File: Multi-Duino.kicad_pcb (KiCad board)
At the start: 4 copper layers, 68.6 x 53.3 mm, 67 parts, among them J1 M20-9980345, J10 Micro_SD_Card_Det1, J2 M20-9980245, J3 M20-9980345, J4 PPTC101LFBN-RC, J5 PPTC081LFBN-RC, J6 PPTC061LFBN-RC, J7 PPTC081LFBN-RC, J8 USB_C_Receptacle_USB2.0_16P, Q1 FDN340P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

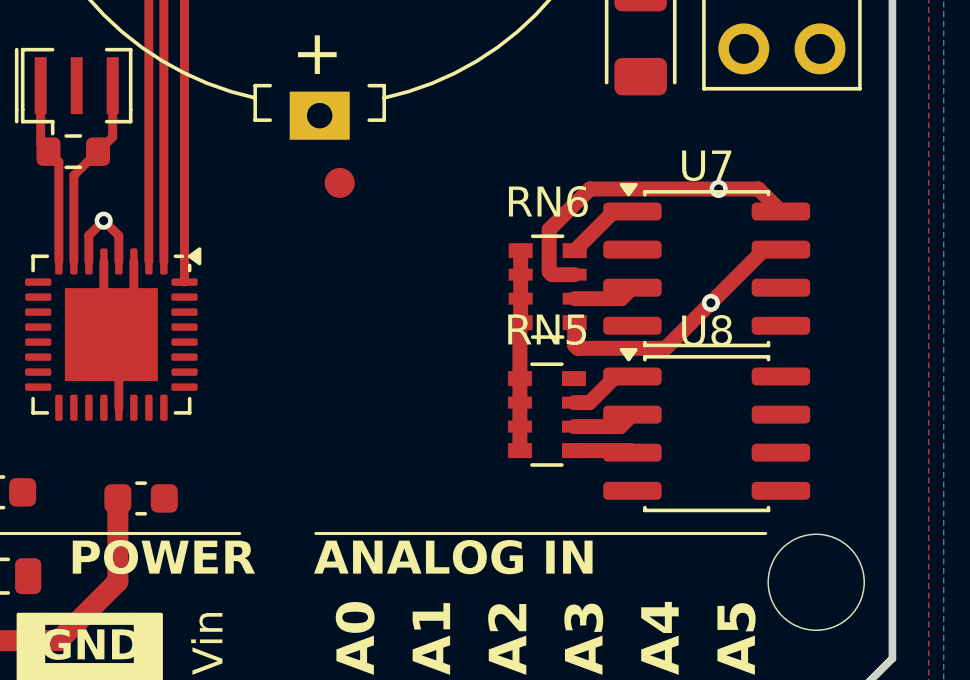
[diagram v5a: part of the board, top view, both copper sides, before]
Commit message: Update Multiduino v2 design
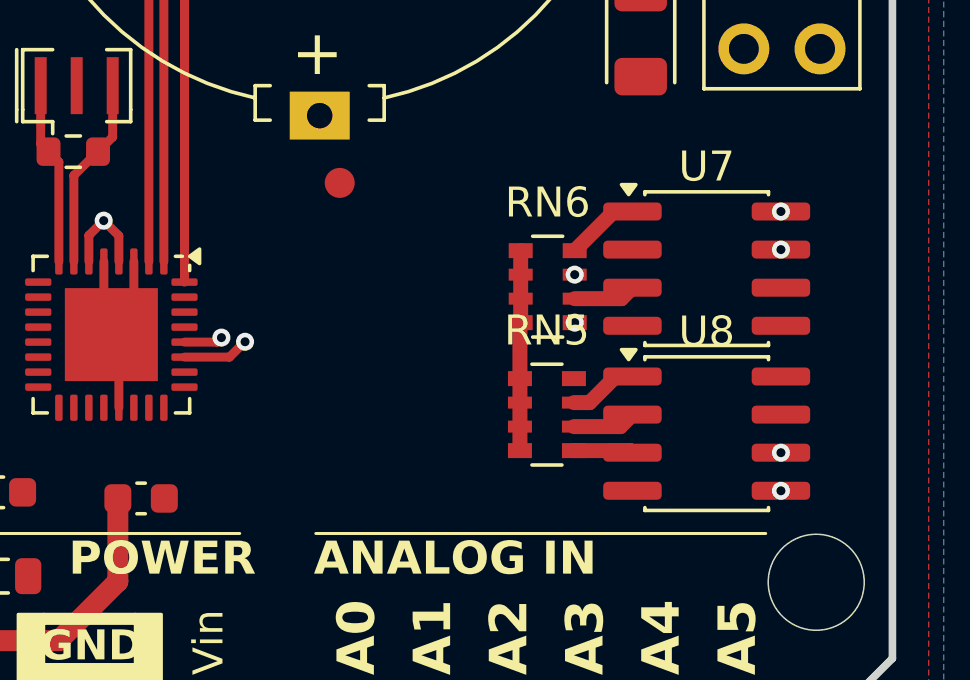
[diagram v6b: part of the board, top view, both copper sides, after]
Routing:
- net A5/SCL: track 10.9 -> 1.29 mm, vias 1 -> 4
- net A4/SDA: track 9.03 -> 2.31 mm, vias 1 -> 4
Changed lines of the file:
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@@
 	)
 	(segment
-		(start 176.741158 114.741158)
-		(end 178.517316 112.965)
-		(width 0.5)
+		(start 160.693801 116.5486)
+		(end 159.1936 116.5486)
+		(width 0.3)
 		(layer "F.Cu")
 		(net 34)
 	)
 	(segment
-		(start 172.2 116.15)
-		(end 172.305 116.255)
-		(width 0.5)
+		(start 161.074562 116.037432)
+		(end 161.074562 116.167839)
+		(width 0.3)
 		(layer "F.Cu")
 		(net 34)
 	)
 	(segment
-		(start 175.227316 116.255)
-		(end 176.741158 114.741158)
-		(width 0.5)
+		(start 161.212426 116.037432)
+		(end 161.074562 116.037432)
+		(width 0.3)
 		(layer "F.Cu")
 		(net 34)
 	)
 	(segment
-		(start 172.305 116.255)
-		(end 175.227316 116.255)
-		(width 0.5)
-		(layer "F.Cu")
-		(net 34)
-	)
-	(segment
-		(start 172.2 115.4)
-		(end 172.2 116.15)
-		(width 0.5)
-		(layer "F.Cu")
-		(net 34)
-	)
-	(segment
-		(start 178.517316 112.965)
-		(end 179.075 112.965)
-		(width 0.5)
+		(start 161.074562 116.167839)
+		(end 160.693801 116.5486)
+		(width 0.3)
 		(layer "F.Cu")
 		(net 34)
 	)
 	(via
-		(at 176.741158 114.741158)
+		(at 172.2 115.4)
+		(size 0.6)
+		(drill 0.3)
+		(layers "F.Cu" "B.Cu")
+		(net 34)
+	)
+	(via
+		(at 161.212426 116.037432)
+		(size 0.6)
+		(drill 0.3)
+		(layers "F.Cu" "B.Cu")
+		(net 34)
+	)
+	(via
+		(at 179.075 112.965)
+		(size 0.6)
+		(drill 0.3)
+		(layers "F.Cu" "B.Cu")
+		(net 34)
+	)
+	(via
+		(at 179.075 121.005)
 		(size 0.6)
 		(drill 0.3)
@@
 	)
 	(segment
-		(start 178.325 110.945)
-		(end 179.075 111.695)
-		(width 0.5)
+		(start 160.274562 116.0486)
+		(end 159.1936 116.0486)
+		(width 0.3)
 		(layer "F.Cu")
 		(net 36)
 	)
 	(segment
-		(start 171.35 113.7)
-		(end 171.35 112.3)
-		(width 0.5)
-		(layer "F.Cu")
-		(net 36)
-	)
-	(segment
-		(start 172.705 110.945)
-		(end 177 110.945)
-		(width 0.5)
-		(layer "F.Cu")
-		(net 36)
-	)
-	(segment
-		(start 177 110.945)
-		(end 178.325 110.945)
-		(width 0.5)
-		(layer "F.Cu")
-		(net 36)
-	)
-	(segment
-		(start 172.2 113.8)
-		(end 171.45 113.8)
-		(width 0.5)
-		(layer "F.Cu")
-		(net 36)
-	)
-	(segment
-		(start 171.35 112.3)
-		(end 172.705 110.945)
-		(width 0.5)
-		(layer "F.Cu")
-		(net 36)
-	)
-	(segment
-		(start 171.45 113.8)
-		(end 171.35 113.7)
-		(width 0.5)
+		(start 160.424562 115.8986)
+		(end 160.274562 116.0486)
+		(width 0.3)
 		(layer "F.Cu")
 		(net 36)
 	)
 	(via
-		(at 177 110.945)
+		(at 160.424562 115.8986)
 		(size 0.6)
 		(drill 0.3)
+		(layers "F.Cu" "B.Cu")
+		(net 36)
+	)
+	(via
+		(at 172.2 113.8)
+		(size 0.6)
+		(drill 0.3)
+		(layers "F.Cu" "B.Cu")
+		(net 36)
+	)
+	(via
+		(at 179.075 111.695)
+		(size 0.6)
+		(drill 0.3)
+		(layers "F.Cu" "B.Cu")
+		(net 36)
+	)
+	(via
+		(at 179.075 119.735)
+		(size 0.6)
+		(drill 0.3)

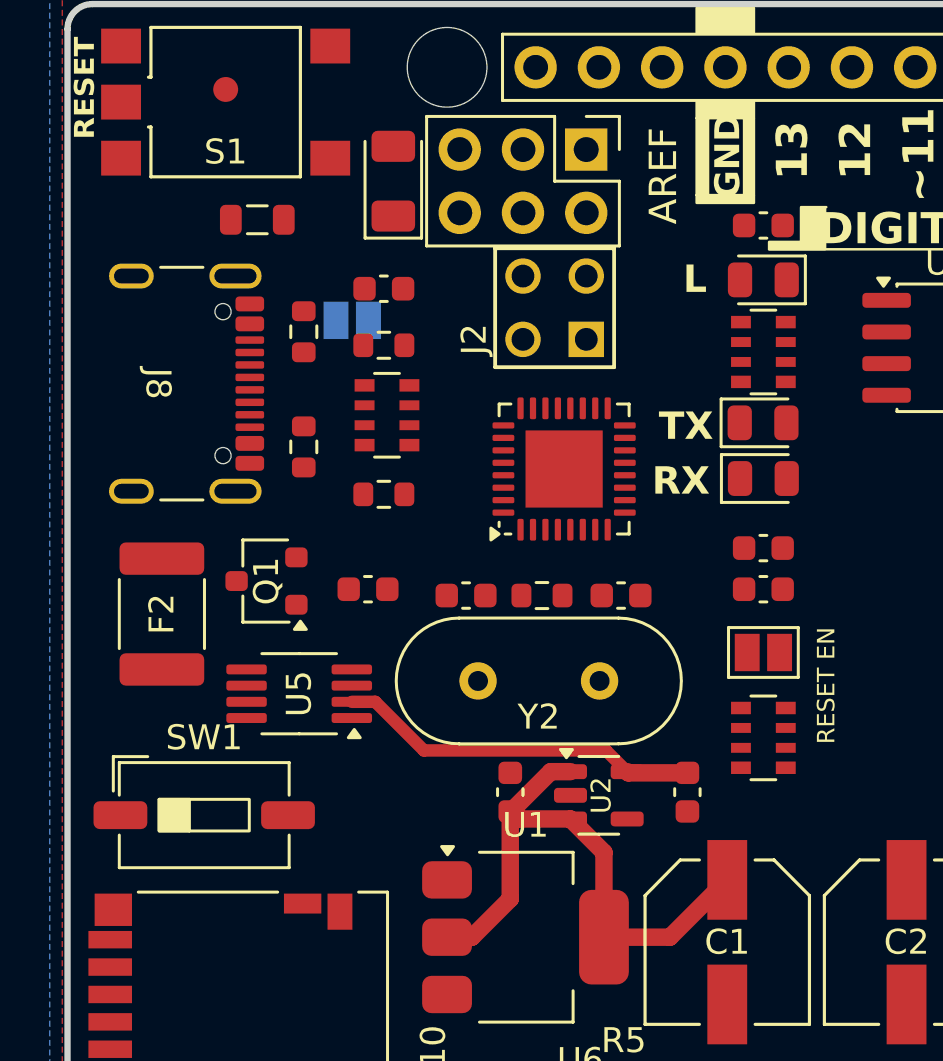
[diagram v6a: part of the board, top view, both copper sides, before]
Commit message: Update Multiduino v2 design
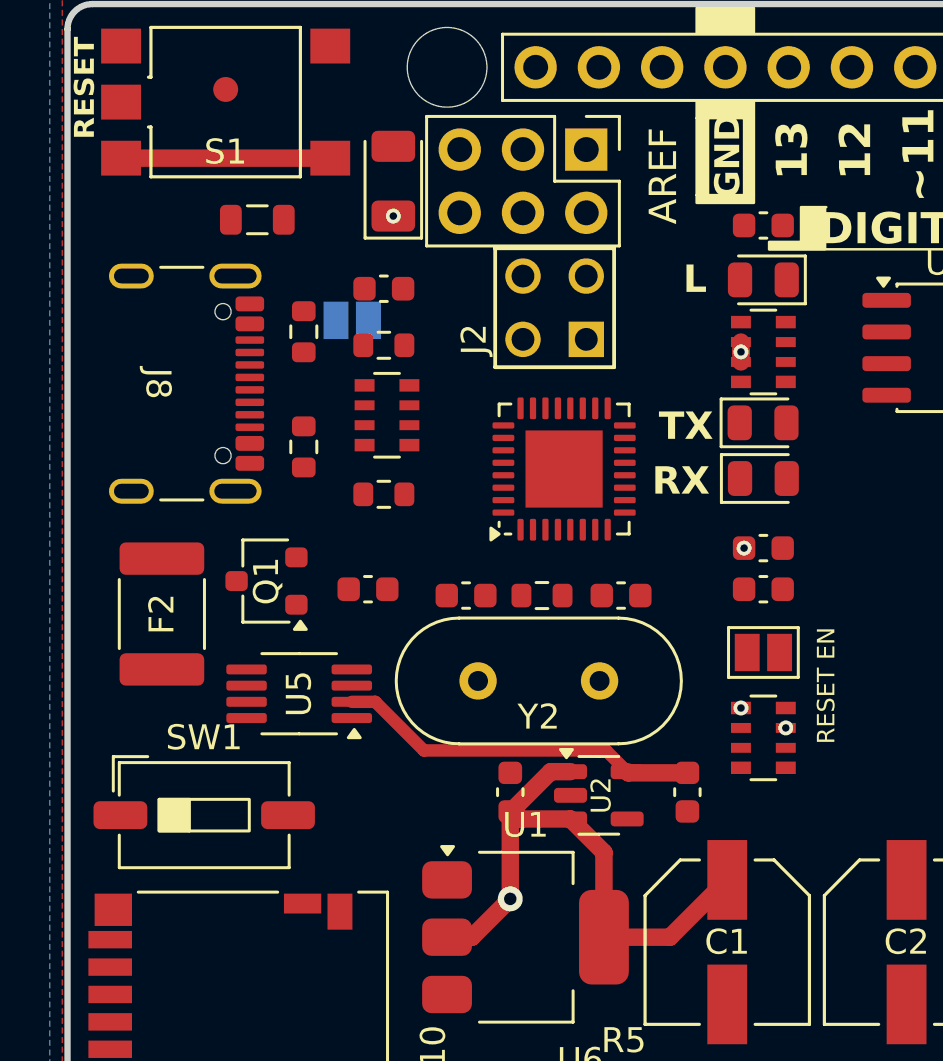
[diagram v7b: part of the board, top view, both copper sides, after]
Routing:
- net RESET: track 0.00 -> 8.40 mm
- net +5V: track 47.0 -> 47.8 mm, vias 1 -> 7
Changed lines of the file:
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@@
+	)
+	(segment
+		(start 141.2511 91.9036)
+		(end 141.2511 92.3)
+		(width 0.7)
+		(layer "F.Cu")
+		(net 2)
 	)
 	(segment
@@
 	)
 	(segment
+		(start 141.2511 92.3)
+		(end 141.2511 92.7036)
+		(width 0.7)
+		(layer "F.Cu")
+		(net 2)
+	)
+	(segment
 		(start 170.4 113.8)
 		(end 170.4 113)
@@
 	)
 	(via
+		(at 141.2511 106.5976)
+		(size 0.6)
+		(drill 0.3)
+		(layers "F.Cu" "B.Cu")
+		(net 2)
+	)
+	(via
+		(at 143.0511 107.3976)
+		(size 0.6)
+		(drill 0.3)
+		(layers "F.Cu" "B.Cu")
+		(net 2)
+	)
+	(via
 		(at 156.5 112)
 		(size 0.6)
 		(drill 0.3)
+		(layers "F.Cu" "B.Cu")
+		(net 2)
+	)
+	(via
+		(at 141.3761 100.1776)
+		(size 0.6)
+		(drill 0.3)
+		(layers "F.Cu" "B.Cu")
+		(net 2)
+	)
+	(via
+		(at 141.2511 92.3)
+		(size 0.6)
+		(drill 0.3)
+		(layers "F.Cu" "B.Cu")
+		(net 2)
+	)
+	(via
+		(at 127.2921 86.8456)
+		(size 0.6)
+		(drill 0.3)
+		(layers "F.Cu" "B.Cu")
+		(net 2)
+	)
+	(via
+		(at 131.988 114.262)
+		(size 1)
+		(drill 0.5)
 		(layers "F.Cu" "B.Cu")
 		(net 2)
@@
 	)
 	(segment
+		(start 116.3611 84.5206)
+		(end 124.7611 84.5206)
+		(width 0.7)
+		(layer "F.Cu")
+		(net 6)
+	)
+	(segment

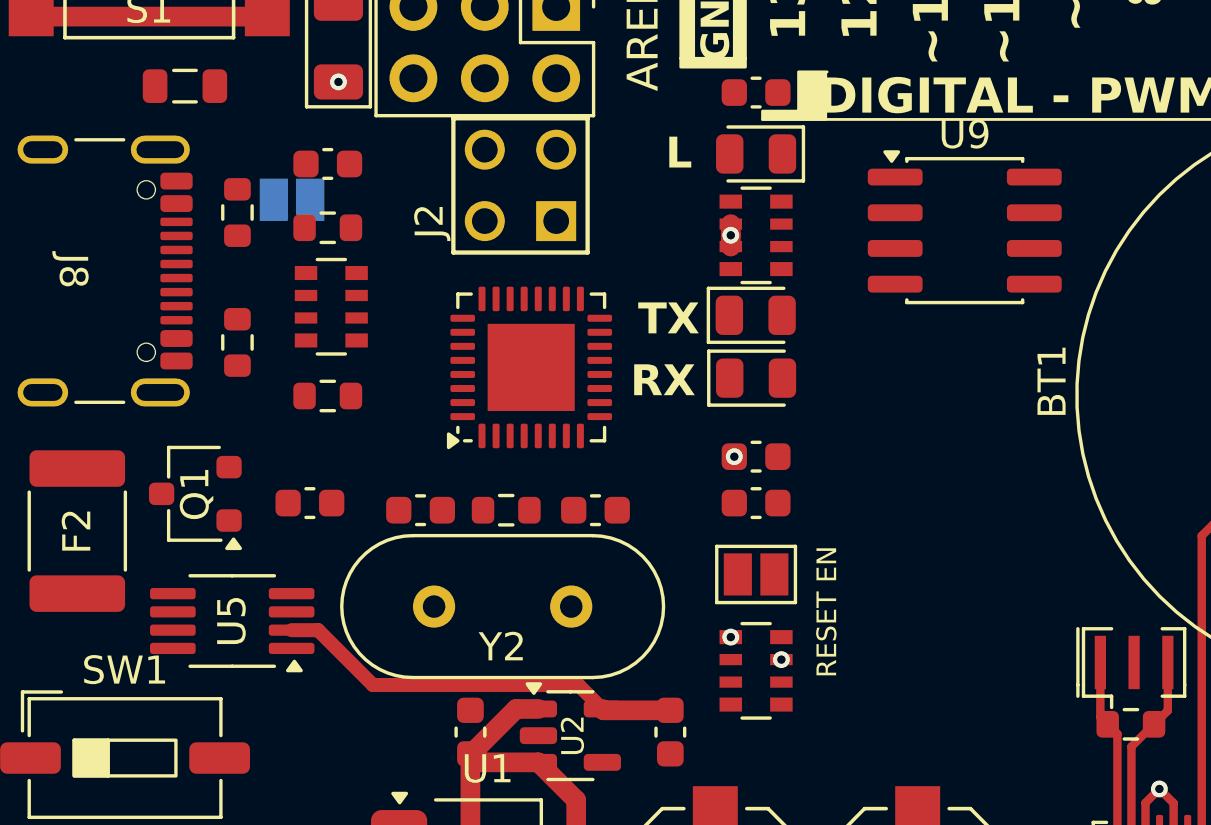
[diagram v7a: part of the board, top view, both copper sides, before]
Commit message: Update Multiduino v2 design
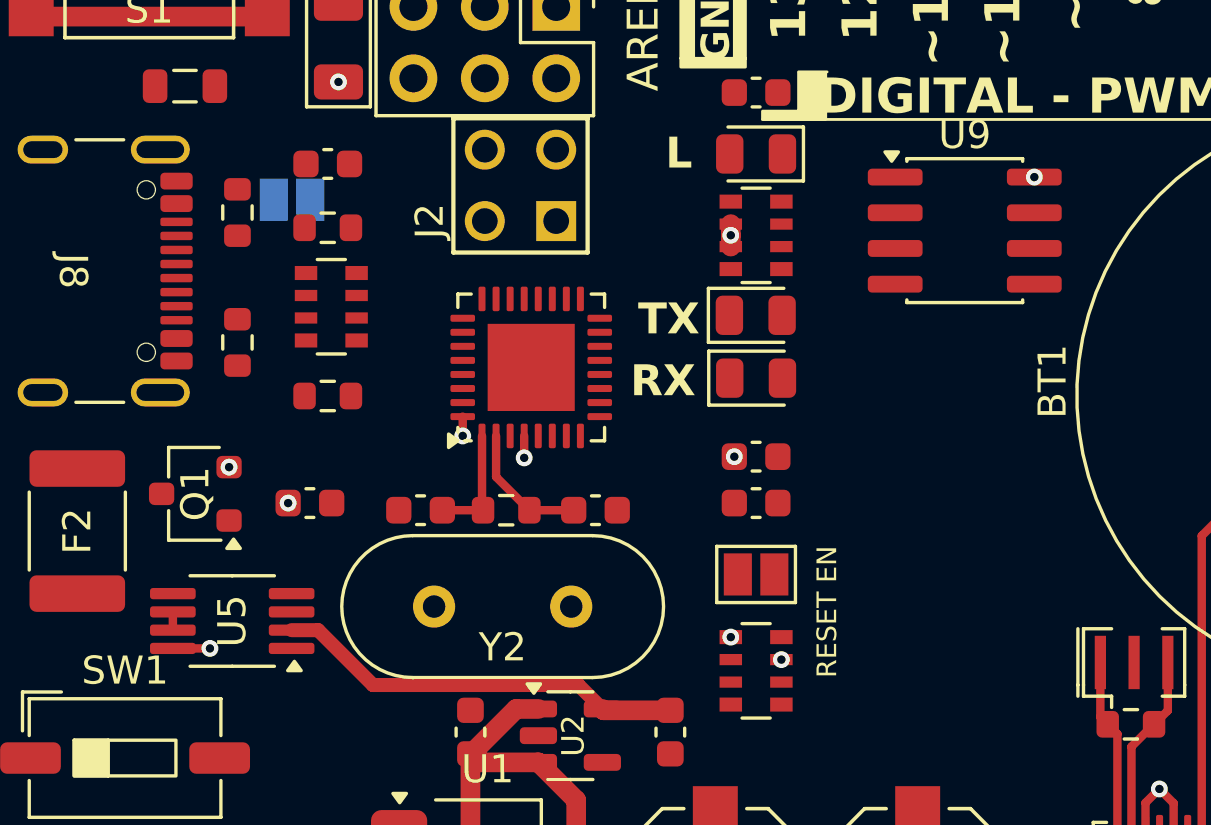
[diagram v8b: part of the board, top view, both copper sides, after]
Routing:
- net Net-(U3-PC0): track 0.00 -> 4.71 mm
- net Net-(U3-XTAL1): track 0.00 -> 4.11 mm
- net +5V: track 47.8 -> 50.6 mm, vias 7 -> 13
- net Net-(RN2A-R1.2): track 0.00 -> 0.65 mm
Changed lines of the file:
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@@
+	)
+	(segment
+		(start 122.72 107)
+		(end 121.4 107)
+		(width 0.3)
+		(layer "F.Cu")
+		(net 2)
 	)
 	(segment
@@
 	)
 	(segment
+		(start 133.9001 100.2201)
+		(end 133.9001 99.4401)
+		(width 0.3)
+		(layer "F.Cu")
+		(net 2)
+	)
+	(segment
 		(start 131.988 110.752)
 		(end 132.01525 110.752)
@@
 	)
 	(segment
+		(start 131.7126 99.44)
+		(end 131.7126 98.7526)
+		(width 0.3)
+		(layer "F.Cu")
+		(net 2)
+	)
+	(segment
 		(start 170.375 119.665)
 		(end 170.375 118.865)
@@
 	)
 	(via
+		(at 131.7126 99.44)
+		(size 0.6)
+		(drill 0.3)
+		(layers "F.Cu" "B.Cu")
+		(net 2)
+	)
+	(via
 		(at 141.2511 106.5976)
 		(size 0.6)
@@
 	)
 	(via
+		(at 123.4 100.55)
+		(size 0.6)
+		(drill 0.3)
+		(layers "F.Cu" "B.Cu")
+		(net 2)
+	)
+	(via
+		(at 122.72 107)
+		(size 0.6)
+		(drill 0.3)
+		(layers "F.Cu" "B.Cu")
+		(net 2)
+	)
+	(via
 		(at 141.3761 100.1776)
 		(size 0.6)
@@
 	)
 	(via
+		(at 133.9001 100.2201)
+		(size 0.6)
+		(drill 0.3)
+		(layers "F.Cu" "B.Cu")
+		(net 2)
+	)
+	(via
 		(at 127.2921 86.8456)
+		(size 0.6)
+		(drill 0.3)
+		(layers "F.Cu" "B.Cu")
+		(net 2)
+	)
+	(via
+		(at 152.05 90.23)
 		(size 0.6)
 		(drill 0.3)
@@
 		(net 2)
 	)
+	(via
+		(at 125.5011 101.8286)
+		(size 0.6)
+		(drill 0.3)
+		(layers "F.Cu" "B.Cu")
+		(net 2)
+	)
 	(segment
 		(start 135.8295 108.302)
@@
 	)
 	(segment
+		(start 132.4361 102.0826)
+		(end 130.9881 102.0826)
+		(width 0.3)
+		(layer "F.Cu")
+		(net 9)
+	)
+	(segment
+		(start 132.4001 102.0466)
+		(end 132.4361 102.0826)
+		(width 0.3)
+		(layer "F.Cu")
+		(net 9)
+	)
+	(segment
+		(start 132.4001 99.4401)
+		(end 132.4001 102.0466)
+		(width 0.3)
+		(layer "F.Cu")
+		(net 9)
+	)
+	(segment
+		(start 132.9001 99.4401)
+		(end 132.9001 100.8966)
+		(width 0.3)
+		(layer "F.Cu")
+		(net 11)
+	)
+	(segment
+		(start 134.0861 102.0826)
+		(end 135.6611 102.0826)
+		(width 0.3)
+		(layer "F.Cu")
+		(net 11)
+	)
+	(segment
+		(start 132.9001 100.8966)
+		(end 134.0861 102.0826)
+		(width 0.3)
+		(layer "F.Cu")
+		(net 11)
+	)
+	(segment
 		(start 160.693801 116.5486)
 		(end 159.1936 116.5486)
@@
 	)
 	(segment
+		(start 121.4 106.35)
+		(end 121.4 105.7)
+		(width 0.3)
+		(layer "F.Cu")
+		(net 61)
+	)
+	(segment
